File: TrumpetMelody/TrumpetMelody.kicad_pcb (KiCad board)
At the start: 2 copper layers, 76.2 x 68.6 mm, 80 parts, among them J1 USB_B_Micro, J2 Conn_01x05, J3 640456-3, J4 640456-3, SW1 SW_Push, U1 STM32F411RETx, U2 TLV62565DBVR, U3 MAX98357AETE_T, U4 MAX7375AXR805

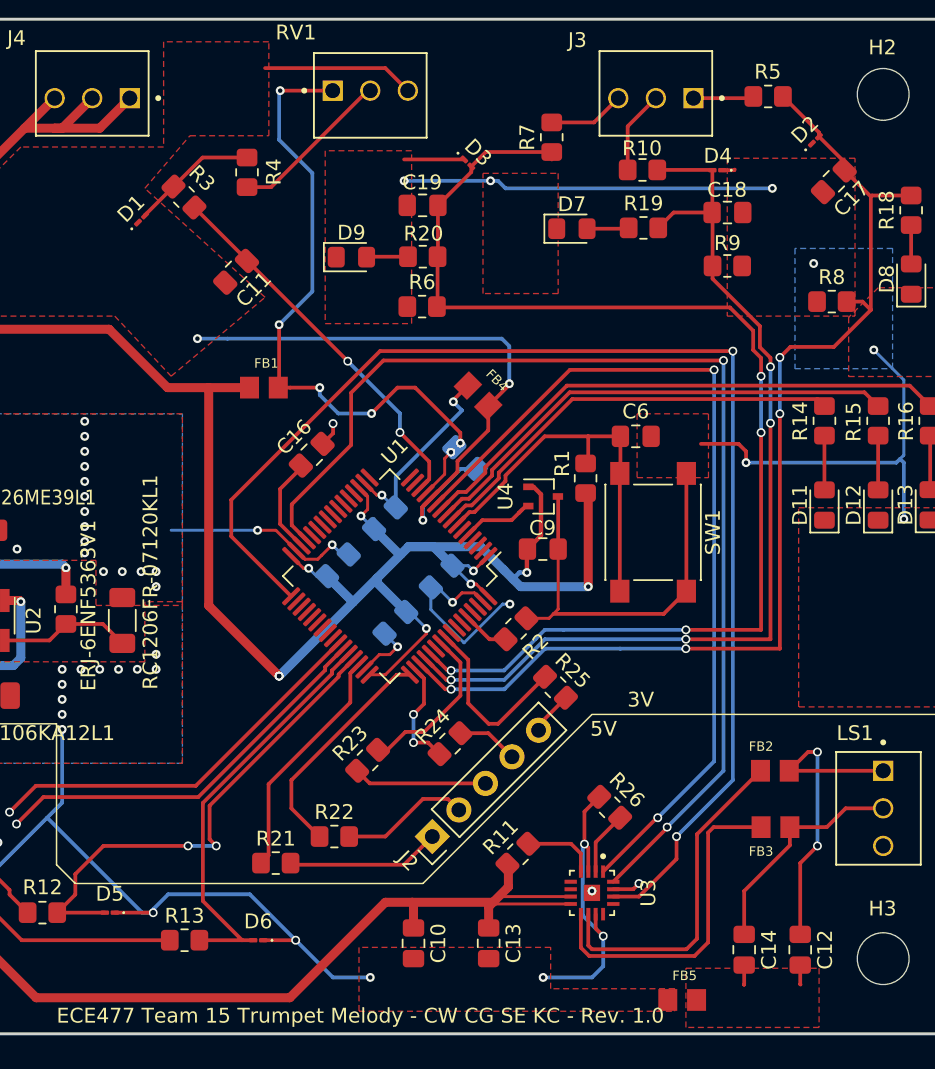
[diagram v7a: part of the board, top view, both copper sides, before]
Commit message: Updated TVS Diodes to be right size and fixed placements
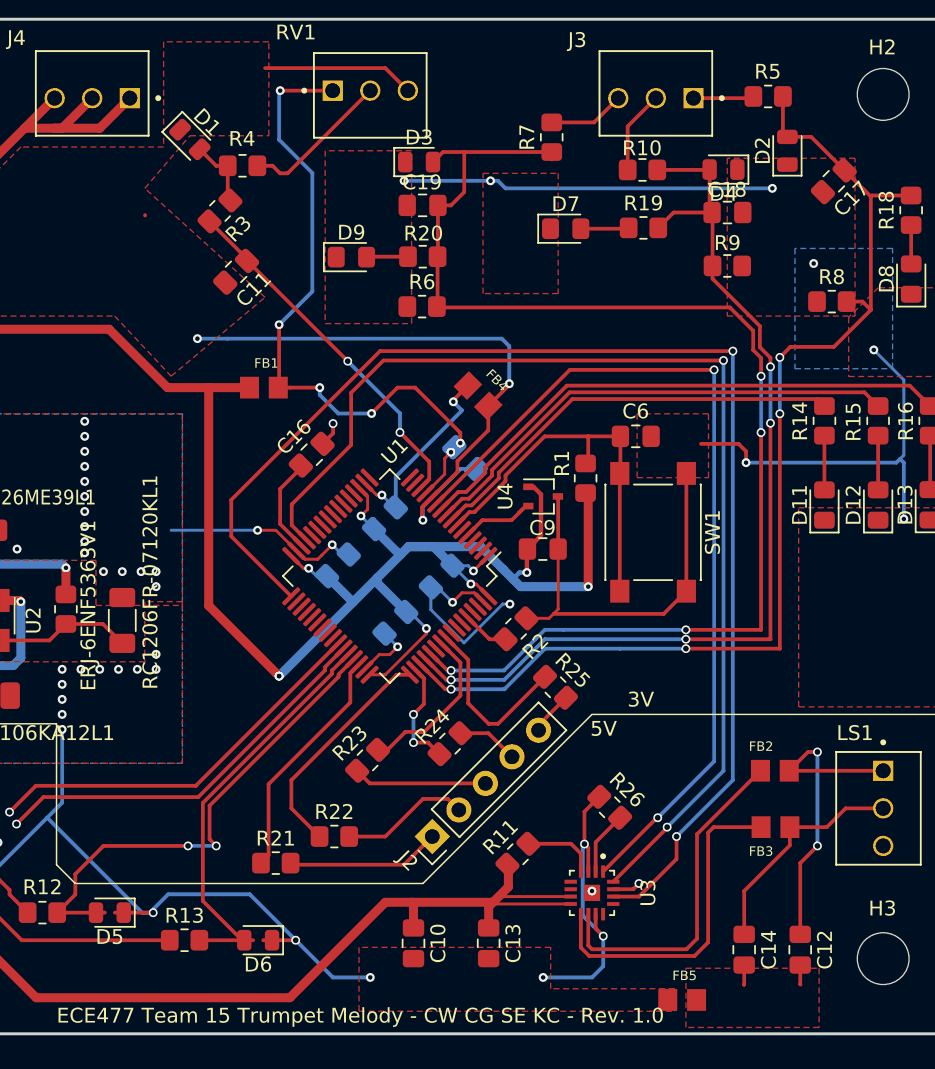
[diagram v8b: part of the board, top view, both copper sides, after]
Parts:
- D1, D2, D3, D4, D5, D6: footprint Diode_SMD:D_01005_0402Metric_Pad0.57x0.30mm_HandSolder -> Diode_SMD:D_0805_2012Metric
- moved D1 6.30 mm to (171.6, 53.8), turned to -45 degrees
- moved D3 3.29 mm to (187.1, 55.4), turned to 0 degrees
- moved R3 2.61 mm to (173.6, 58.7), turned to 45 degrees
- moved D2 2.03 mm to (212.0, 54.6), turned to 90 degrees
- moved R4 0.54 mm to (175.1, 55.6), turned to 0 degrees
- moved D7 0.42 mm to (197.0, 59.9)
- moved D4 0.42 mm to (207.6, 55.9)
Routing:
- net GND: track 211.5 -> 206.6 mm
- net Net-(D1-A2): track 8.54 -> 4.77 mm
- net GPIO_BUTTON_2: track 83.1 -> 86.9 mm
- net GPIO_BUTTON_0: track 74.8 -> 76.3 mm
- net ADC1_IN0: track 25.8 -> 24.4 mm
- net Net-(R4-Pad2): track 11.0 -> 10.3 mm
